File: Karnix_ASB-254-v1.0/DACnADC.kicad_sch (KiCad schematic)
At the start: 83 parts, among them U10 ADC128S052CIMT, U11 AD5328BRUZ, U12 LM258A, U13 LM258A, U14 LM258A, U15 LM258A, U16 LM258A

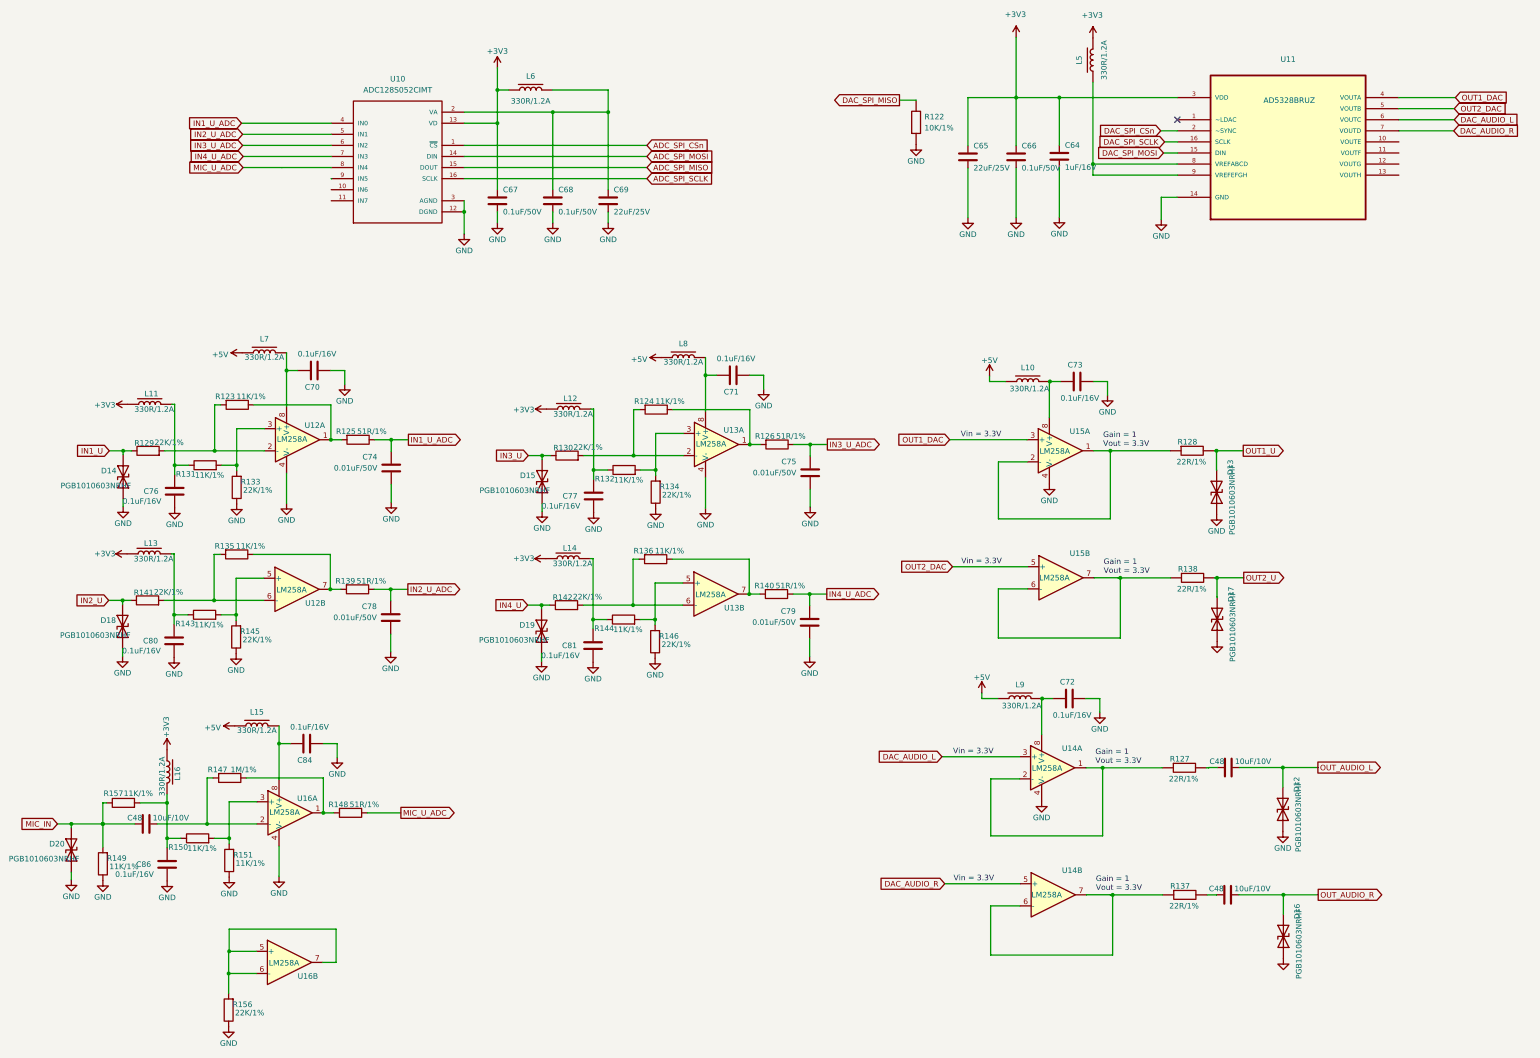
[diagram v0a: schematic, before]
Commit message: Optimize component base
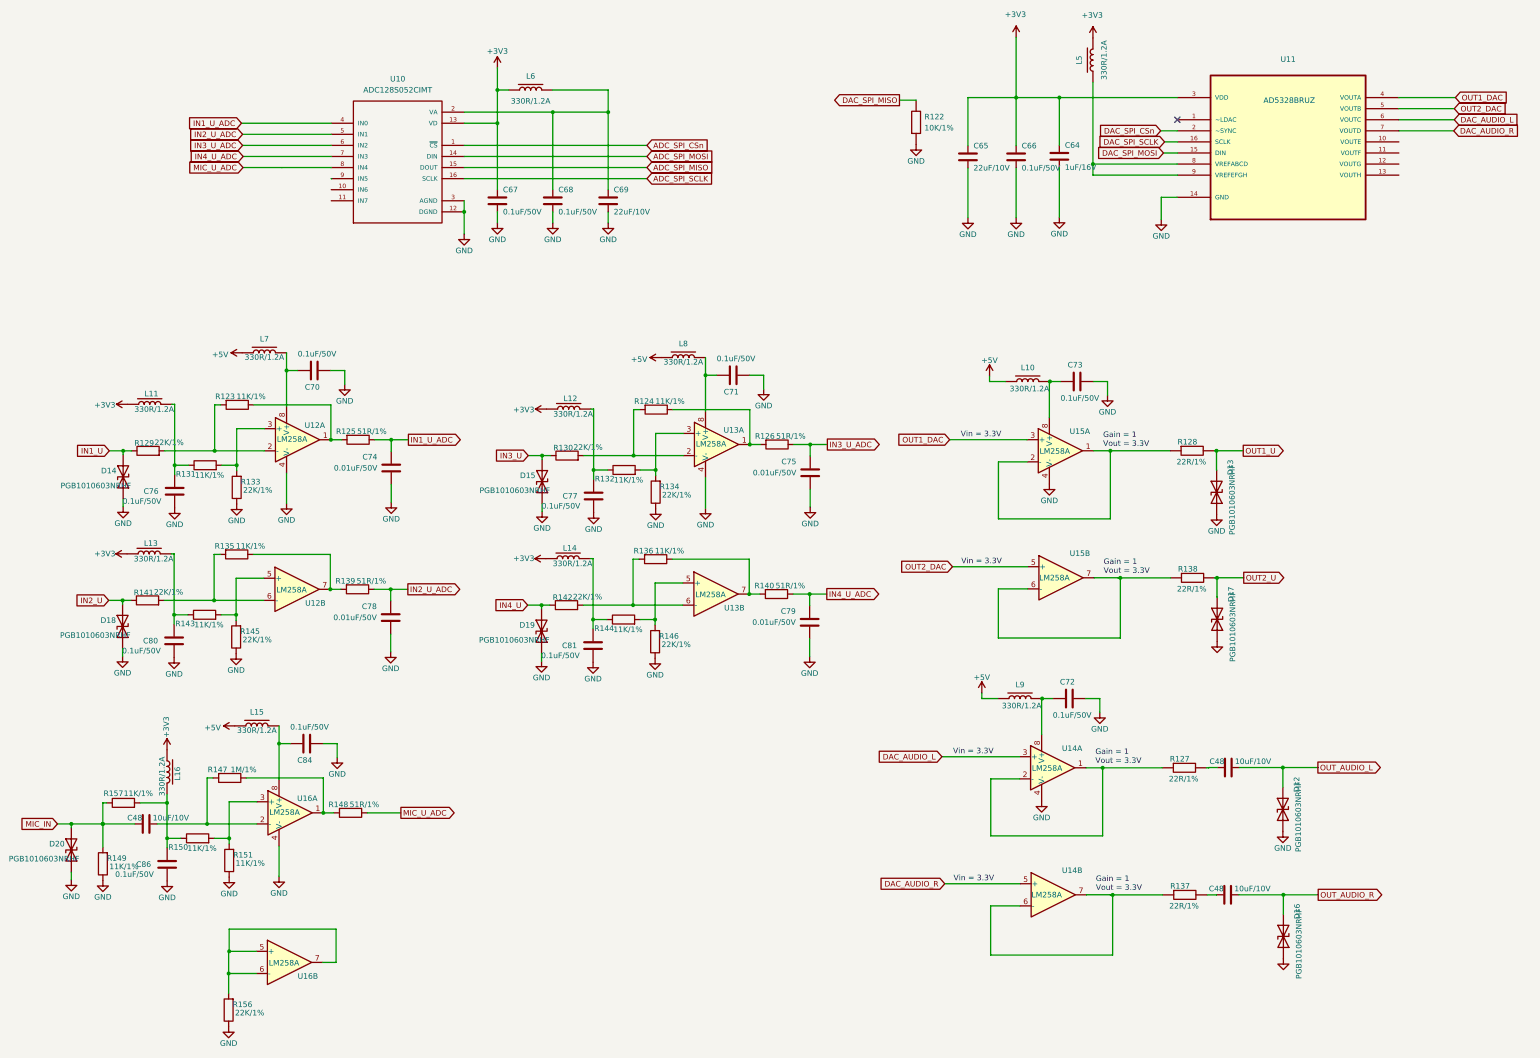
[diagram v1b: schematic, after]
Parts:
- C65, C69: value 22uF/25V -> 22uF/10V; Mfr. Part Number C2220C226J3RACTU -> TCC0805X5R226M100FT
- C66, C67, C68: footprint Fabmicro:C_0402_1005Metric -> Capacitor_SMD:C_0402_1005Metric
- C70, C71, C72, C73, C76, C77, C80, C81, C84, C86: value 0.1uF/16V -> 0.1uF/50V; Mfr. Part Number CL05B104K05NNNC -> CC0402KRX7R9BB104
- U11: MPN AD5328BRUZ -> (none); Mfr. Part Number (none) -> AD5328BRUZ
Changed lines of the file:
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@@
   (title_block
     (title "ПИР СЦХ-254 \"Карно\"\n(Karnix ASB-254)")
-    (date "2023-10-20")
+    (date "2023-10-21")
     (rev "V1.0")
     (company "ООО \"Фабмикро\"")
@@
       (effects (font (size 1.27 1.27)) (justify left))
     )
-    (property "Value" "0.1uF/16V" (at 58.365 134.167 0)
+    (property "Value" "0.1uF/50V" (at 58.365 134.167 0)
       (effects (font (size 1.27 1.27)) (justify left))
     )
@@
       (effects (font (size 1.27 1.27)) hide)
     )
-    (property "Mfr. Part Number" "CL05B104K05NNNC" (at 61.413 131.881 0)
+    (property "Mfr. Part Number" "CC0402KRX7R9BB104" (at 61.413 131.881 0)
       (effects (font (size 1.27 1.27)) hide)
     )
@@
       (effects (font (size 1.27 1.27)) (justify left))
     )
-    (property "Footprint" "Fabmicro:C_0402_1005Metric" (at 149.0752 69.09 90)
+    (property "Footprint" "Capacitor_SMD:C_0402_1005Metric" (at 149.0752 69.09 90)
       (effects (font (size 1.27 1.27)) hide)
     )
@@
       (effects (font (size 1.27 1.27)) (justify left))
     )
-    (property "Value" "0.1uF/16V" (at 58.238 168.457 0)
+    (property "Value" "0.1uF/50V" (at 58.238 168.457 0)
       (effects (font (size 1.27 1.27)) (justify left))
     )
@@
       (effects (font (size 1.27 1.27)) hide)
     )
-    (property "Mfr. Part Number" "CL05B104K05NNNC" (at 61.286 166.171 0)
+    (property "Mfr. Part Number" "CC0402KRX7R9BB104" (at 61.286 166.171 0)
       (effects (font (size 1.27 1.27)) hide)
     )
@@
       (effects (font (size 1.27 1.27)) (justify left))
     )
-    (property "Footprint" "Fabmicro:C_0402_1005Metric" (at 136.3752 69.09 90)
+    (property "Footprint" "Capacitor_SMD:C_0402_1005Metric" (at 136.3752 69.09 90)
       (effects (font (size 1.27 1.27)) hide)
     )
@@
       (effects (font (size 1.27 1.27)) (justify left))
     )
-    (property "Value" "0.1uF/16V" (at 271.6209 183.2167 90)
+    (property "Value" "0.1uF/50V" (at 271.6209 183.2167 90)
       (effects (font (size 1.27 1.27)) (justify left))
     )
@@
       (effects (font (size 1.27 1.27)) hide)
     )
-    (property "Mfr. Part Number" "CL05B104K05NNNC" (at 266.5409 179.4067 0)
+    (property "Mfr. Part Number" "CC0402KRX7R9BB104" (at 266.5409 179.4067 0)
       (effects (font (size 1.27 1.27)) hide)
     )
@@
       (effects (font (size 1.27 1.27)) (justify left))
     )
-    (property "Value" "0.1uF/16V" (at 273.3922 110.5301 90)
+    (property "Value" "0.1uF/50V" (at 273.3922 110.5301 90)
       (effects (font (size 1.27 1.27)) (justify left))
     )
@@
       (effects (font (size 1.27 1.27)) hide)
     )
-    (property "Mfr. Part Number" "CL05B104K05NNNC" (at 268.3122 106.7201 0)
+    (property "Mfr. Part Number" "CC0402KRX7R9BB104" (at 268.3122 106.7201 0)
       (effects (font (size 1.27 1.27)) hide)
     )
@@
       (effects (font (size 1.27 1.27)) (justify left))
     )
-    (property "Value" "0.1uF/16V" (at 96.774 185.928 90)
+    (property "Value" "0.1uF/50V" (at 96.774 185.928 90)
       (effects (font (size 1.27 1.27)) (justify left))
     )
@@
       (effects (font (size 1.27 1.27)) hide)
     )
-    (property "Mfr. Part Number" "CL05B104K05NNNC" (at 91.694 189.738 0)
+    (property "Mfr. Part Number" "CC0402KRX7R9BB104" (at 91.694 189.738 0)
       (effects (font (size 1.27 1.27)) hide)
     )
@@
       (effects (font (size 1.27 1.27)) (justify left))
     )
-    (property "Value" "0.1uF/16V" (at 154.295 169.546 0)
+    (property "Value" "0.1uF/50V" (at 154.295 169.546 0)
       (effects (font (size 1.27 1.27)) (justify left))
     )
@@
       (effects (font (size 1.27 1.27)) hide)
     )
-    (property "Mfr. Part Number" "CL05B104K05NNNC" (at 157.343 167.26 0)
+    (property "Mfr. Part Number" "CC0402KRX7R9BB104" (at 157.343 167.26 0)
       (effects (font (size 1.27 1.27)) hide)
     )
@@
       (effects (font (size 1.27 1.27)) (justify left))
     )
-    (property "Value" "0.1uF/16V" (at 98.497 100.385 90)
+    (property "Value" "0.1uF/50V" (at 98.497 100.385 90)
       (effects (font (size 1.27 1.27)) (justify left))
     )
@@
       (effects (font (size 1.27 1.27)) hide)
     )
-    (property "Mfr. Part Number" "CL05B104K05NNNC" (at 93.417 104.195 0)
+    (property "Mfr. Part Number" "CC0402KRX7R9BB104" (at 93.417 104.195 0)
       (effects (font (size 1.27 1.27)) hide)
     )
@@
       (effects (font (size 1.27 1.27)) (justify left))
     )
-    (property "Value" "22uF/25V" (at 244.564 57.749 90)
+    (property "Value" "22uF/10V" (at 244.564 57.749 90)
       (effects (font (size 1.27 1.27)) (justify left))
     )
@@
       (effects (font (size 1.27 1.27)) hide)
     )
-    (property "Mfr. Part Number" "C2220C226J3RACTU" (at 243.294 55.209 0)
+    (property "Mfr. Part Number" "TCC0805X5R226M100FT" (at 243.294 55.209 0)
       (effects (font (size 1.27 1.27)) hide)
     )
@@
       (effects (font (size 1.27 1.27)) (justify left))
     )
-    (property "Value" "22uF/25V" (at 162.08 67.82 90)
+    (property "Value" "22uF/10V" (at 162.08 67.82 90)
       (effects (font (size 1.27 1.27)) (justify left))
     )
@@
       (effects (font (size 1.27 1.27)) hide)
     )
-    (property "Mfr. Part Number" "C2220C226J3RACTU" (at 160.81 65.28 0)
+    (property "Mfr. Part Number" "TCC0805X5R226M100FT" (at 160.81 65.28 0)
       (effects (font (size 1.27 1.27)) hide)
     )
@@
       (effects (font (size 1.27 1.27)) (justify left))
     )
-    (property "Footprint" "Fabmicro:C_0402_1005Metric" (at 255.3082 59.019 90)
+    (property "Footprint" "Capacitor_SMD:C_0402_1005Metric" (at 255.3082 59.019 90)
       (effects (font (size 1.27 1.27)) hide)
     )
@@
       (effects (font (size 1.27 1.27)) (justify left))
     )
-    (property "Value" "0.1uF/16V" (at 194.554 101.474 90)
+    (property "Value" "0.1uF/50V" (at 194.554 101.474 90)
       (effects (font (size 1.27 1.27)) (justify left))
     )
@@
       (effects (font (size 1.27 1.27)) hide)
     )
-    (property "Mfr. Part Number" "CL05B104K05NNNC" (at 189.474 105.284 0)
+    (property "Mfr. Part Number" "CC0402KRX7R9BB104" (at 189.474 105.284 0)
       (effects (font (size 1.27 1.27)) hide)
     )
@@
       (effects (font (size 1.27 1.27)) (justify left))
     )
-    (property "Value" "0.1uF/16V" (at 56.642 219.71 0)
+    (property "Value" "0.1uF/50V" (at 56.642 219.71 0)
       (effects (font (size 1.27 1.27)) (justify left))
     )
@@
       (effects (font (size 1.27 1.27)) hide)
     )
-    (property "Mfr. Part Number" "CL05B104K05NNNC" (at 59.69 217.424 0)
+    (property "Mfr. Part Number" "CC0402KRX7R9BB104" (at 59.69 217.424 0)
       (effects (font (size 1.27 1.27)) hide)
     )
@@
       (effects (font (size 1.27 1.27)) (justify left))
     )
-    (property "Value" "0.1uF/16V" (at 154.422 135.256 0)
+    (property "Value" "0.1uF/50V" (at 154.422 135.256 0)
       (effects (font (size 1.27 1.27)) (justify left))
     )
@@
       (effects (font (size 1.27 1.27)) hide)
     )
-    (property "Mfr. Part Number" "CL05B104K05NNNC" (at 157.47 132.97 0)
+    (property "Mfr. Part Number" "CC0402KRX7R9BB104" (at 157.47 132.97 0)
       (effects (font (size 1.27 1.27)) hide)
     )
@@
       (effects (font (size 1.27 1.27)) (justify bottom) hide)
     )
-    (property "MPN" "AD5328BRUZ" (at 316.7 49.24 0)
+    (property "Mfr. Part Number" "AD5328BRUZ" (at 316.7 49.24 0)
       (effects (font (size 1.27 1.27)) (justify bottom) hide)
     )
